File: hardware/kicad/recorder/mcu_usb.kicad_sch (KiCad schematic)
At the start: 11 parts, among them J1 UART0, J2 USB_C_16P, U1 ESP32-S3-MINI-1U-N8, U7 USBLC6-2SC6

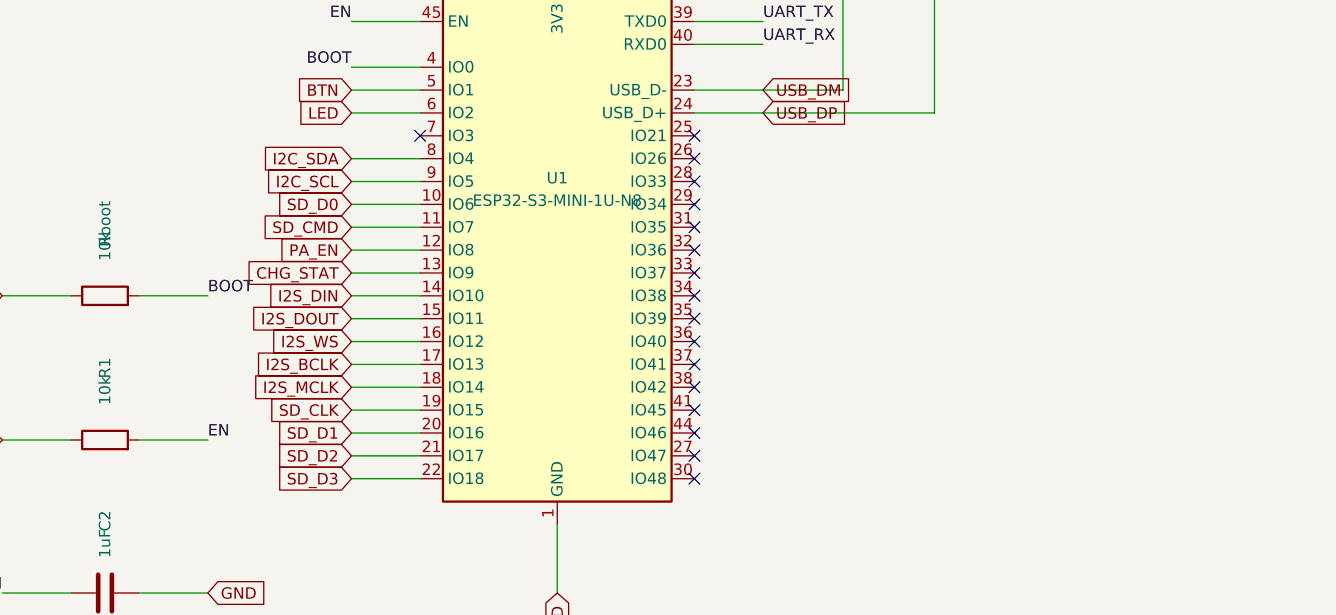
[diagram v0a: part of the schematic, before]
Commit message: Add SMT Boot and Reset buttons so the board can enter download mode after USB mass-storage owns the port.
Co-authored-by: Cursor <cursoragent@cursor.com>
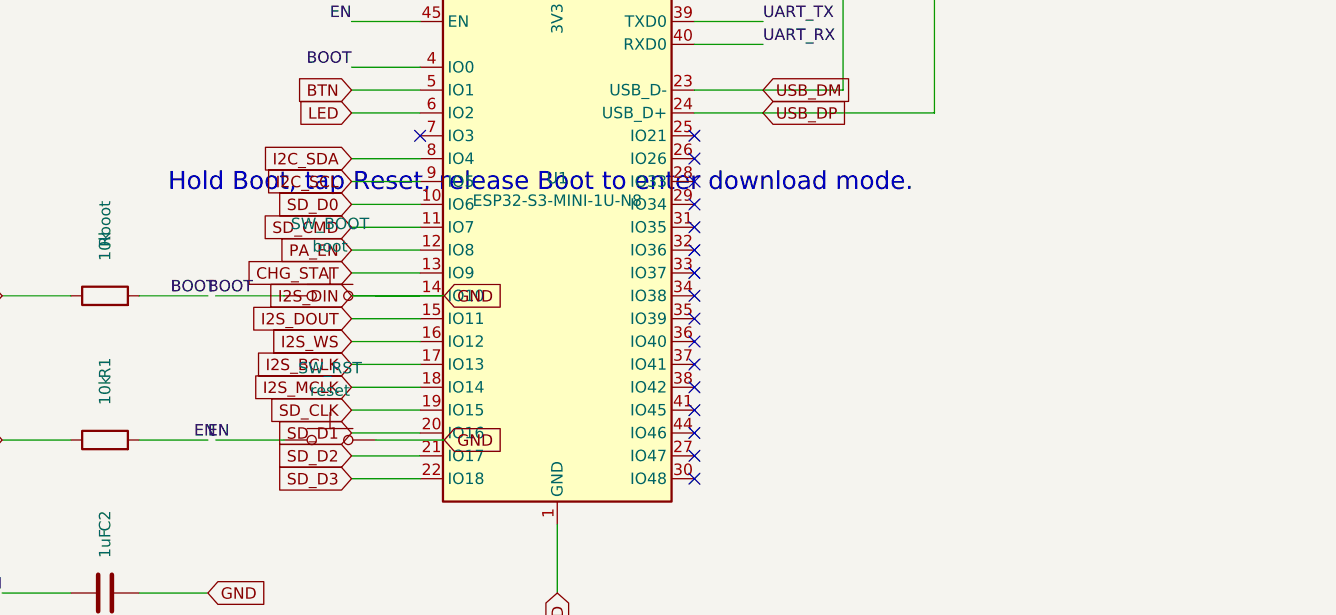
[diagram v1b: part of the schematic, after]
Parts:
- added SW_BOOT: boot, Button_Switch_SMD:SW_Push_1P1T_XKB_TS-1187A, symbol Switch:SW_Push
- added SW_RST: reset, Button_Switch_SMD:SW_Push_1P1T_XKB_TS-1187A, symbol Switch:SW_Push
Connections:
- net I2S_DIN is gone; now on net GND: U1.14 (IO10)
- net BOOT: now also SW_BOOT.1
- net EN: now also SW_RST.1
- net GND: now also SW_BOOT.2, SW_RST.2
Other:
- note added: "Hold Boot, tap Reset, release Boot to enter download mode."
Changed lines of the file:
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@@
 		(effects (font (size 1.27 1.27)) (justify left bottom))
+	)
+	(symbol
+		(lib_id "Switch:SW_Push")
+		(at 70.00 119.38 0)
+		(unit 1)
+		(exclude_from_sim no)
+		(in_bom yes)
+		(on_board yes)
+		(dnp no)
+		(property "Reference" "SW_BOOT" (at 70.00 111.38 0)
+			(effects (font (size 1.27 1.27))))
+		(property "Value" "boot" (at 70.00 113.88 0)
+			(effects (font (size 1.27 1.27))))
+		(property "Footprint" "Button_Switch_SMD:SW_Push_1P1T_XKB_TS-1187A" (at 70.00 119.38 0)
+			(effects (font (size 1.27 1.27)) hide))
+		(property "Datasheet" "~" (at 70.00 119.38 0)
+			(effects (font (size 1.27 1.27)) hide))
+		(pin "1")
+		(pin "2")
+	)
+	(wire
+		(pts (xy 64.92 119.38) (xy 57.30 119.38))
+		(stroke (width 0) (type default))
+	)
+	(label "BOOT"
+		(at 57.30 119.38 180)
+		(effects (font (size 1.27 1.27)) (justify right bottom))
+	)
+	(wire
+		(pts (xy 75.08 119.38) (xy 82.70 119.38))
+		(stroke (width 0) (type default))
+	)
+	(global_label "GND"
+		(shape input)
+		(at 82.70 119.38 0)
+		(effects (font (size 1.27 1.27)) (justify left))
+	)
+	(symbol
+		(lib_id "Switch:SW_Push")
+		(at 70.00 135.40 0)
+		(unit 1)
+		(exclude_from_sim no)
+		(in_bom yes)
+		(on_board yes)
+		(dnp no)
+		(property "Reference" "SW_RST" (at 70.00 127.40 0)
+			(effects (font (size 1.27 1.27))))
+		(property "Value" "reset" (at 70.00 129.90 0)
+			(effects (font (size 1.27 1.27))))
+		(property "Footprint" "Button_Switch_SMD:SW_Push_1P1T_XKB_TS-1187A" (at 70.00 135.40 0)
+			(effects (font (size 1.27 1.27)) hide))
+		(property "Datasheet" "~" (at 70.00 135.40 0)
+			(effects (font (size 1.27 1.27)) hide))
+		(pin "1")
+		(pin "2")
+	)
+	(wire
+		(pts (xy 64.92 135.40) (xy 57.30 135.40))
+		(stroke (width 0) (type default))
+	)
+	(label "EN"
+		(at 57.30 135.40 180)
+		(effects (font (size 1.27 1.27)) (justify right bottom))
+	)
+	(wire
+		(pts (xy 75.08 135.40) (xy 82.70 135.40))
+		(stroke (width 0) (type default))
+	)
+	(global_label "GND"
+		(shape input)
+		(at 82.70 135.40 0)
+		(effects (font (size 1.27 1.27)) (justify left))
+	)
+	(text "Hold Boot, tap Reset, release Boot to enter download mode."
+		(exclude_from_sim no)
+		(at 52.00 108.00 0)
+		(effects (font (size 2.0 2.0)) (justify left bottom))
 	)
 	(wire
